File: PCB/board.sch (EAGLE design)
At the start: 37 parts, among them IC1 W25Q32JVSSIQ, J1 USB-TYPE-C-31-M-12, Q1 S8050, Q2 S8050, U1 AMS1117_SOT223, U2 CH340C, U3 ESP8266EX, X1 SMA, Y1 40Mhz

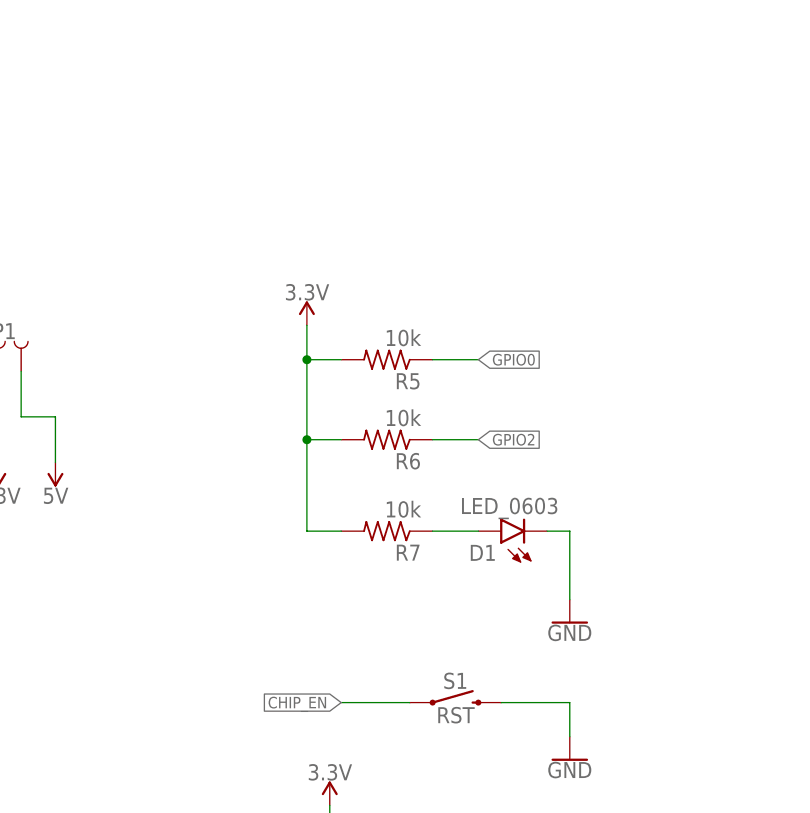
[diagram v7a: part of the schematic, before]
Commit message: GPIO15 pull-down
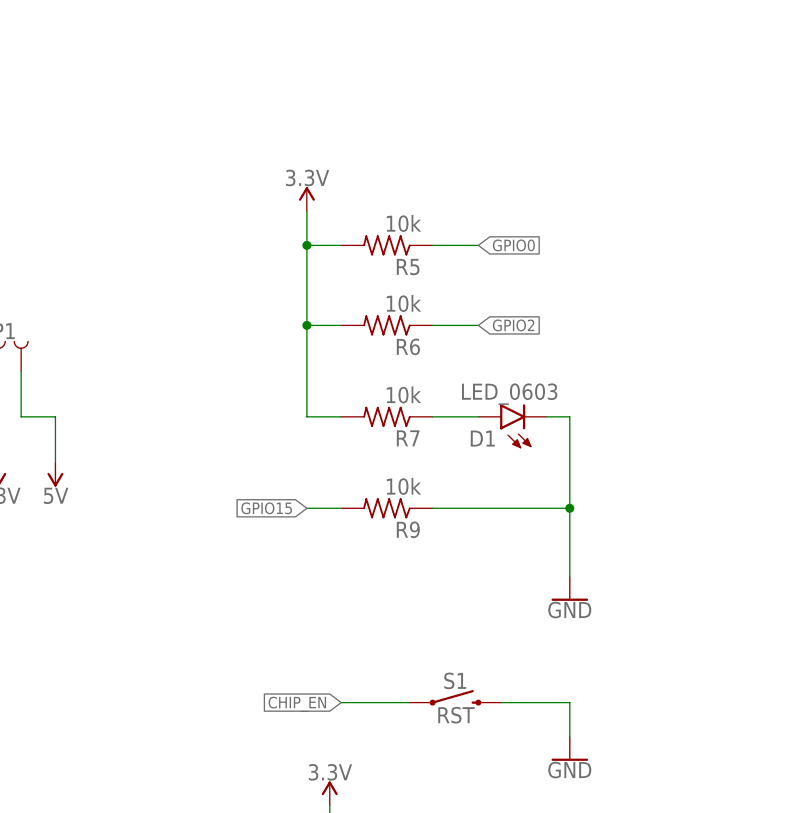
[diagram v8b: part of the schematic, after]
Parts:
- added R9: 10k, angrypig7-RCL:RR0402
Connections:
- net GND: now also R9.1
- net GPIO15: now also R9.2
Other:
- moved on the sheet: D1, R5, R6, R7
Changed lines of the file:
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@@
 </part>
 <part name="SUPPLY6" library="SparkFun-PowerSymbols" deviceset="3.3V" device=""/>
+<part name="R9" library="angrypig7-RCL" deviceset="R" device="R0402" package3d_urn="urn:adsk.eagle:package:23547/3" value="10k">
+<spice>
+<pinmapping spiceprefix="R">
+<pinmap gate="G$1" pin="1" pinorder="1"/>
+<pinmap gate="G$1" pin="2" pinorder="2"/>
+</pinmapping>
+</spice>
+<attribute name="LCSC" value="C25744"/>
+</part>
 </parts>
 <sheets>
@@
 <attribute name="VALUE" x="138.43" y="74.676" size="1.778" layer="96" align="top-center"/>
 </instance>
-<instance part="R7" gate="G$1" x="118.11" y="100.33" smashed="yes" rot="R180">
-<attribute name="NAME" x="121.92" y="98.8314" size="1.778" layer="95" rot="R180"/>
-<attribute name="VALUE" x="121.92" y="103.632" size="1.778" layer="96" rot="R180"/>
-<attribute name="LCSC" x="118.11" y="100.33" size="1.27" layer="96" rot="R180" display="off"/>
-</instance>
-<instance part="D1" gate="G$1" x="132.08" y="100.33" smashed="yes" rot="R180">
-<attribute name="NAME" x="130.302" y="98.806" size="1.778" layer="95" rot="R180"/>
-<attribute name="VALUE" x="126.238" y="102.235" size="1.778" layer="96"/>
-<attribute name="LCSC" x="132.08" y="100.33" size="1.27" layer="96" rot="R180" display="off"/>
-</instance>
-<instance part="GND21" gate="1" x="138.43" y="90.17" smashed="yes">
-<attribute name="VALUE" x="138.43" y="89.916" size="1.778" layer="96" align="top-center"/>
-</instance>
-<instance part="SUPPLY15" gate="G$1" x="109.22" y="123.19" smashed="yes">
-<attribute name="VALUE" x="109.22" y="125.984" size="1.778" layer="96" align="bottom-center"/>
+<instance part="R7" gate="G$1" x="118.11" y="113.03" smashed="yes" rot="R180">
+<attribute name="NAME" x="121.92" y="111.5314" size="1.778" layer="95" rot="R180"/>
+<attribute name="VALUE" x="121.92" y="116.332" size="1.778" layer="96" rot="R180"/>
+<attribute name="LCSC" x="118.11" y="113.03" size="1.27" layer="96" rot="R180" display="off"/>
+</instance>
+<instance part="D1" gate="G$1" x="132.08" y="113.03" smashed="yes" rot="R180">
+<attribute name="NAME" x="130.302" y="111.506" size="1.778" layer="95" rot="R180"/>
+<attribute name="VALUE" x="126.238" y="114.935" size="1.778" layer="96"/>
+<attribute name="LCSC" x="132.08" y="113.03" size="1.27" layer="96" rot="R180" display="off"/>
+</instance>
+<instance part="GND21" gate="1" x="138.43" y="92.71" smashed="yes">
+<attribute name="VALUE" x="138.43" y="92.456" size="1.778" layer="96" align="top-center"/>
+</instance>
+<instance part="SUPPLY15" gate="G$1" x="109.22" y="135.89" smashed="yes">
+<attribute name="VALUE" x="109.22" y="138.684" size="1.778" layer="96" align="bottom-center"/>
 </instance>
 <instance part="JP1" gate="A" x="21.59" y="118.11" smashed="yes" rot="R180">
@@
 <attribute name="VALUE" x="243.84" y="196.596" size="1.778" layer="96" align="top-center"/>
 </instance>
-<instance part="R5" gate="G$1" x="118.11" y="119.38" smashed="yes" rot="R180">
-<attribute name="NAME" x="121.92" y="117.8814" size="1.778" layer="95" rot="R180"/>
-<attribute name="VALUE" x="121.92" y="122.682" size="1.778" layer="96" rot="R180"/>
-<attribute name="LCSC" x="118.11" y="119.38" size="1.27" layer="96" rot="R180" display="off"/>
-</instance>
-<instance part="R6" gate="G$1" x="118.11" y="110.49" smashed="yes" rot="R180">
-<attribute name="NAME" x="121.92" y="108.9914" size="1.778" layer="95" rot="R180"/>
-<attribute name="VALUE" x="121.92" y="113.792" size="1.778" layer="96" rot="R180"/>
-<attribute name="LCSC" x="118.11" y="110.49" size="1.27" layer="96" rot="R180" display="off"/>
+<instance part="R5" gate="G$1" x="118.11" y="132.08" smashed="yes" rot="R180">
+<attribute name="NAME" x="121.92" y="130.5814" size="1.778" layer="95" rot="R180"/>
+<attribute name="VALUE" x="121.92" y="135.382" size="1.778" layer="96" rot="R180"/>
+<attribute name="LCSC" x="118.11" y="132.08" size="1.27" layer="96" rot="R180" display="off"/>
+</instance>
+<instance part="R6" gate="G$1" x="118.11" y="123.19" smashed="yes" rot="R180">
+<attribute name="NAME" x="121.92" y="121.6914" size="1.778" layer="95" rot="R180"/>
+<attribute name="VALUE" x="121.92" y="126.492" size="1.778" layer="96" rot="R180"/>
+<attribute name="LCSC" x="118.11" y="123.19" size="1.27" layer="96" rot="R180" display="off"/>
 </instance>
 <instance part="U2" gate="G$1" x="44.45" y="175.26" smashed="yes">
@@
 <instance part="SUPPLY6" gate="G$1" x="13.97" y="184.15" smashed="yes">
 <attribute name="VALUE" x="13.97" y="186.944" size="1.778" layer="96" align="bottom-center"/>
+</instance>
+<instance part="R9" gate="G$1" x="118.11" y="102.87" smashed="yes" rot="R180">
+<attribute name="NAME" x="121.92" y="101.3714" size="1.778" layer="95" rot="R180"/>
+<attribute name="VALUE" x="121.92" y="106.172" size="1.778" layer="96" rot="R180"/>
+<attribute name="LCSC" x="118.11" y="102.87" size="1.27" layer="96" rot="R180" display="off"/>
 </instance>
 </instances>
@@
 <segment>
 <pinref part="GND21" gate="1" pin="GND"/>
-<wire x1="138.43" y1="92.71" x2="138.43" y2="100.33" width="0.1524" layer="91"/>
+<wire x1="138.43" y1="95.25" x2="138.43" y2="102.87" width="0.1524" layer="91"/>
 <pinref part="D1" gate="G$1" pin="C"/>
-<wire x1="138.43" y1="100.33" x2="135.89" y2="100.33" width="0.1524" layer="91"/>
+<wire x1="138.43" y1="102.87" x2="138.43" y2="113.03" width="0.1524" layer="91"/>
+<wire x1="138.43" y1="113.03" x2="135.89" y2="113.03" width="0.1524" layer="91"/>
+<pinref part="R9" gate="G$1" pin="1"/>
+<wire x1="123.19" y1="102.87" x2="138.43" y2="102.87" width="0.1524" layer="91"/>
+<junction x="138.43" y="102.87"/>
 </segment>
 <segment>
@@
 <segment>
 <pinref part="R7" gate="G$1" pin="2"/>
-<wire x1="113.03" y1="100.33" x2="109.22" y2="100.33" width="0.1524" layer="91"/>
+<wire x1="113.03" y1="113.03" x2="109.22" y2="113.03" width="0.1524" layer="91"/>
 <pinref part="SUPPLY15" gate="G$1" pin="3.3V"/>
-<wire x1="109.22" y1="100.33" x2="109.22" y2="110.49" width="0.1524" layer="91"/>
-<wire x1="109.22" y1="110.49" x2="109.22" y2="119.38" width="0.1524" layer="91"/>
-<wire x1="109.22" y1="119.38" x2="109.22" y2="123.19" width="0.1524" layer="91"/>
+<wire x1="109.22" y1="113.03" x2="109.22" y2="123.19" width="0.1524" layer="91"/>
+<wire x1="109.22" y1="123.19" x2="109.22" y2="132.08" width="0.1524" layer="91"/>
+<wire x1="109.22" y1="132.08" x2="109.22" y2="135.89" width="0.1524" layer="91"/>
 <pinref part="R6" gate="G$1" pin="2"/>
-<wire x1="113.03" y1="110.49" x2="109.22" y2="110.49" width="0.1524" layer="91"/>
-<junction x="109.22" y="110.49"/>
+<wire x1="113.03" y1="123.19" x2="109.22" y2="123.19" width="0.1524" layer="91"/>
+<junction x="109.22" y="123.19"/>
 <pinref part="R5" gate="G$1" pin="2"/>
-<wire x1="113.03" y1="119.38" x2="109.22" y2="119.38" width="0.1524" layer="91"/>
-<junction x="109.22" y="119.38"/>
+<wire x1="113.03" y1="132.08" x2="109.22" y2="132.08" width="0.1524" layer="91"/>
+<junction x="109.22" y="132.08"/>
 </segment>
 <segment>
@@
 <label x="304.8" y="128.27" size="1.27" layer="95" rot="R270" xref="yes"/>
 </segment>
+<segment>
+<pinref part="R9" gate="G$1" pin="2"/>
+<wire x1="113.03" y1="102.87" x2="109.22" y2="102.87" width="0.1524" layer="91"/>
+<label x="109.22" y="102.87" size="1.27" layer="95" rot="R180" xref="yes"/>
+</segment>
 </net>
 <net name="GPIO2" class="0">
@@
 <segment>
 <pinref part="R6" gate="G$1" pin="1"/>
-<wire x1="123.19" y1="110.49" x2="128.27" y2="110.49" width="0.1524" layer="91"/>
-<label x="128.27" y="110.49" size="1.27" layer="95" xref="yes"/>
+<wire x1="123.19" y1="123.19" x2="128.27" y2="123.19" width="0.1524" layer="91"/>
+<label x="128.27" y="123.19" size="1.27" layer="95" xref="yes"/>
 </segment>
 </net>
@@
 <segment>
 <pinref part="R5" gate="G$1" pin="1"/>
-<wire x1="123.19" y1="119.38" x2="128.27" y2="119.38" width="0.1524" layer="91"/>
-<label x="128.27" y="119.38" size="1.27" layer="95" xref="yes"/>
+<wire x1="123.19" y1="132.08" x2="128.27" y2="132.08" width="0.1524" layer="91"/>
+<label x="128.27" y="132.08" size="1.27" layer="95" xref="yes"/>
 </segment>
 <segment>
@@
 <pinref part="D1" gate="G$1" pin="A"/>
 <pinref part="R7" gate="G$1" pin="1"/>
-<wire x1="128.27" y1="100.33" x2="123.19" y2="100.33" width="0.1524" layer="91"/>
-</segment>
-</net>
+<wire x1="128.27" y1="113.03" x2="123.19" y2="113.03" width="0.1524" layer="91"/>
+</segment>
+</net>
